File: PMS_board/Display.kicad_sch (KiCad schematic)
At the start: 0 parts

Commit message: added buzzer? looked into stuff
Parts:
- added B1: Buzzer, symbol MRDT_Devices:Buzzer
- added D9: RED, symbol Device:LED
- added Q1: BSS138, Package_TO_SOT_SMD:SOT-23, symbol Transistor_FET:BSS138
- added R3: 2.2k, symbol Device:R_US
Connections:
- new net: B1.2 (V-), D9.1 (K), Q1.3 (D)
- new net: D9.2 (A), R3.2
- new net +3V3: B1.1 (V+), R3.1
- new net BuzzerSignal: Q1.1 (G)
- new net GND: Q1.2 (S)

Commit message: TryingToFigureOutRoveNode
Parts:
- added D10, D11: Green, symbol Device:LED
- added D12: Yellow, symbol Device:LED
- added D13: Red, symbol Device:LED
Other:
- moved on the sheet: B1, D9, Q1, R3

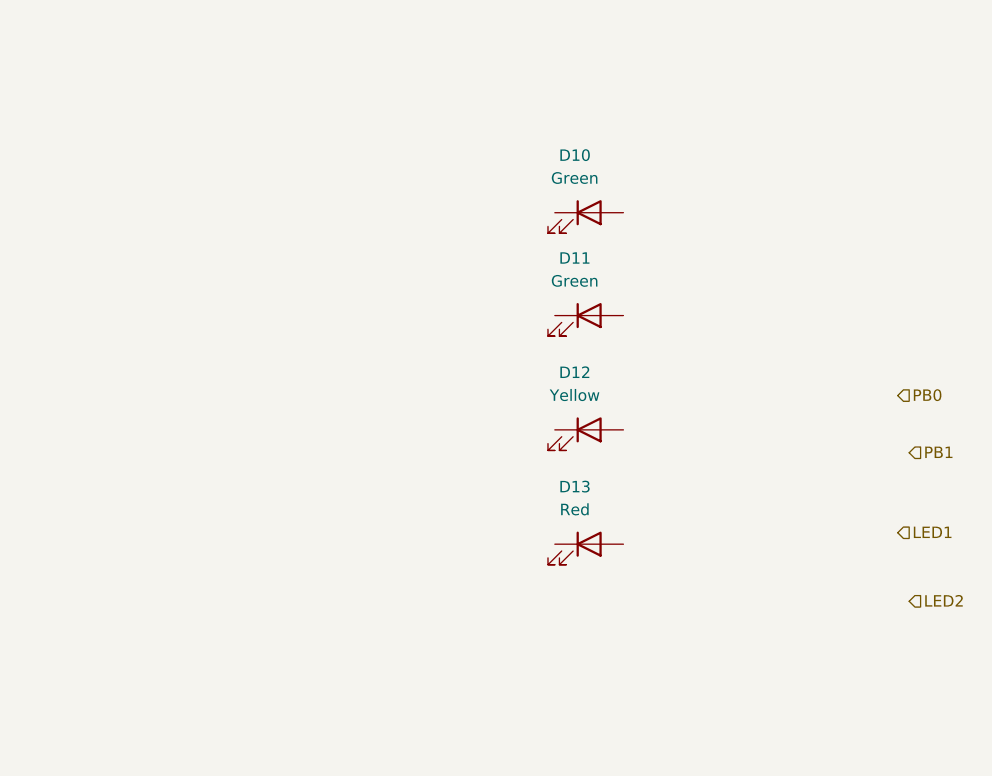
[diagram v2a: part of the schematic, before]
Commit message: addeddisplay
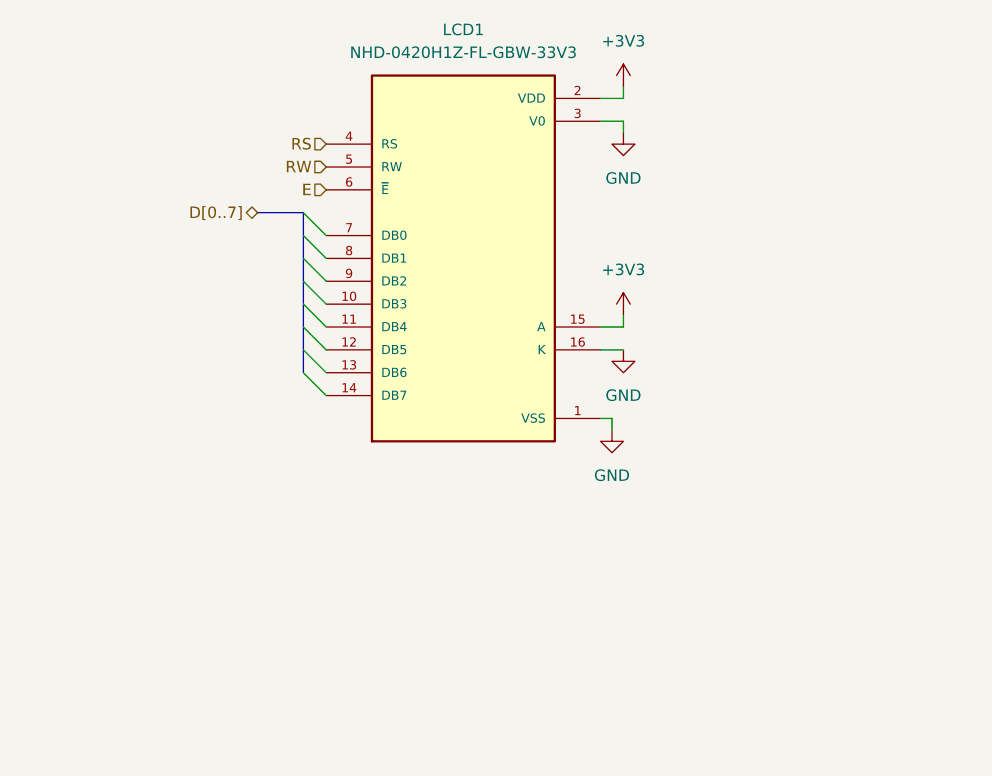
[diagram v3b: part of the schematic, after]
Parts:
- removed D10, D11: Green, symbol Device:LED
- removed D12: Yellow, symbol Device:LED
- removed D13: Red, symbol Device:LED
- added LCD1: NHD-0420H1Z-FL-GBW-33V3, NHD-0420H1Z-FL-GBW-33V3:LCD_NHD-0420H1Z-FL-GBW-33V3, symbol NHD-0420H1Z-FL-GBW-33V3:NHD-0420H1Z-FL-GBW-33V3
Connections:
- net +3V3: now also LCD1.15 (A), LCD1.2 (VDD)
- net GND: now also LCD1.1 (VSS), LCD1.16 (K), LCD1.3 (V0)
- new net E: LCD1.6 (~{E})
- new net RS: LCD1.4 (RS)
- new net RW: LCD1.5 (RW)
